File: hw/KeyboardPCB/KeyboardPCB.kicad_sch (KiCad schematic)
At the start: 176 parts, among them IC1 TPS2113ADRBR, IC2 BGM220PC22HNA2R, J1 USB_B_Micro, J2 Conn_01x07_Pin, J3 Conn_01x06_Pin, J4 Conn_02x05_Odd_Even, J5 BATT_POS, J6 BATT_NEG, K1 KEYSW, K10 KEYSW, K11 KEYSW, K12 KEYSW, K13 KEYSW, K14 KEYSW, K15 KEYSW, K16 KEYSW, K17 KEYSW, K18 KEYSW, K19 KEYSW, K2 KEYSW, K20 KEYSW, K21 KEYSW, K22 KEYSW, K23 KEYSW, K24 KEYSW, K25 KEYSW, K26 KEYSW, K27 KEYSW, K28 KEYSW, K29 KEYSW, K3 KEYSW, K30 KEYSW, K31 KEYSW, K32 KEYSW, K33 KEYSW, K34 KEYSW, K35 KEYSW, K36 KEYSW, K37 KEYSW, K38 KEYSW, K39 KEYSW, K4 KEYSW, K40 KEYSW, K41 KEYSW, K42 KEYSW, K43 KEYSW, K44 KEYSW, K45 KEYSW, K46 KEYSW, K47 KEYSW, K48 KEYSW, K49 KEYSW, K5 KEYSW, K50 KEYSW, K51 KEYSW, K52 KEYSW, K53 KEYSW, K54 KEYSW, K55 KEYSW, K56 KEYSW, K57 KEYSW, K58 KEYSW, K59 KEYSW, K6 KEYSW, K60 KEYSW, K61 KEYSW, K62 KEYSW, K7 KEYSW, K8 KEYSW, K9 KEYSW, SW2 BAT_SWITCH, U1 TM4C123GH6PMI7, U2 TPS73633DBV, U3 Adafruit ST7735R, X2 16MHz

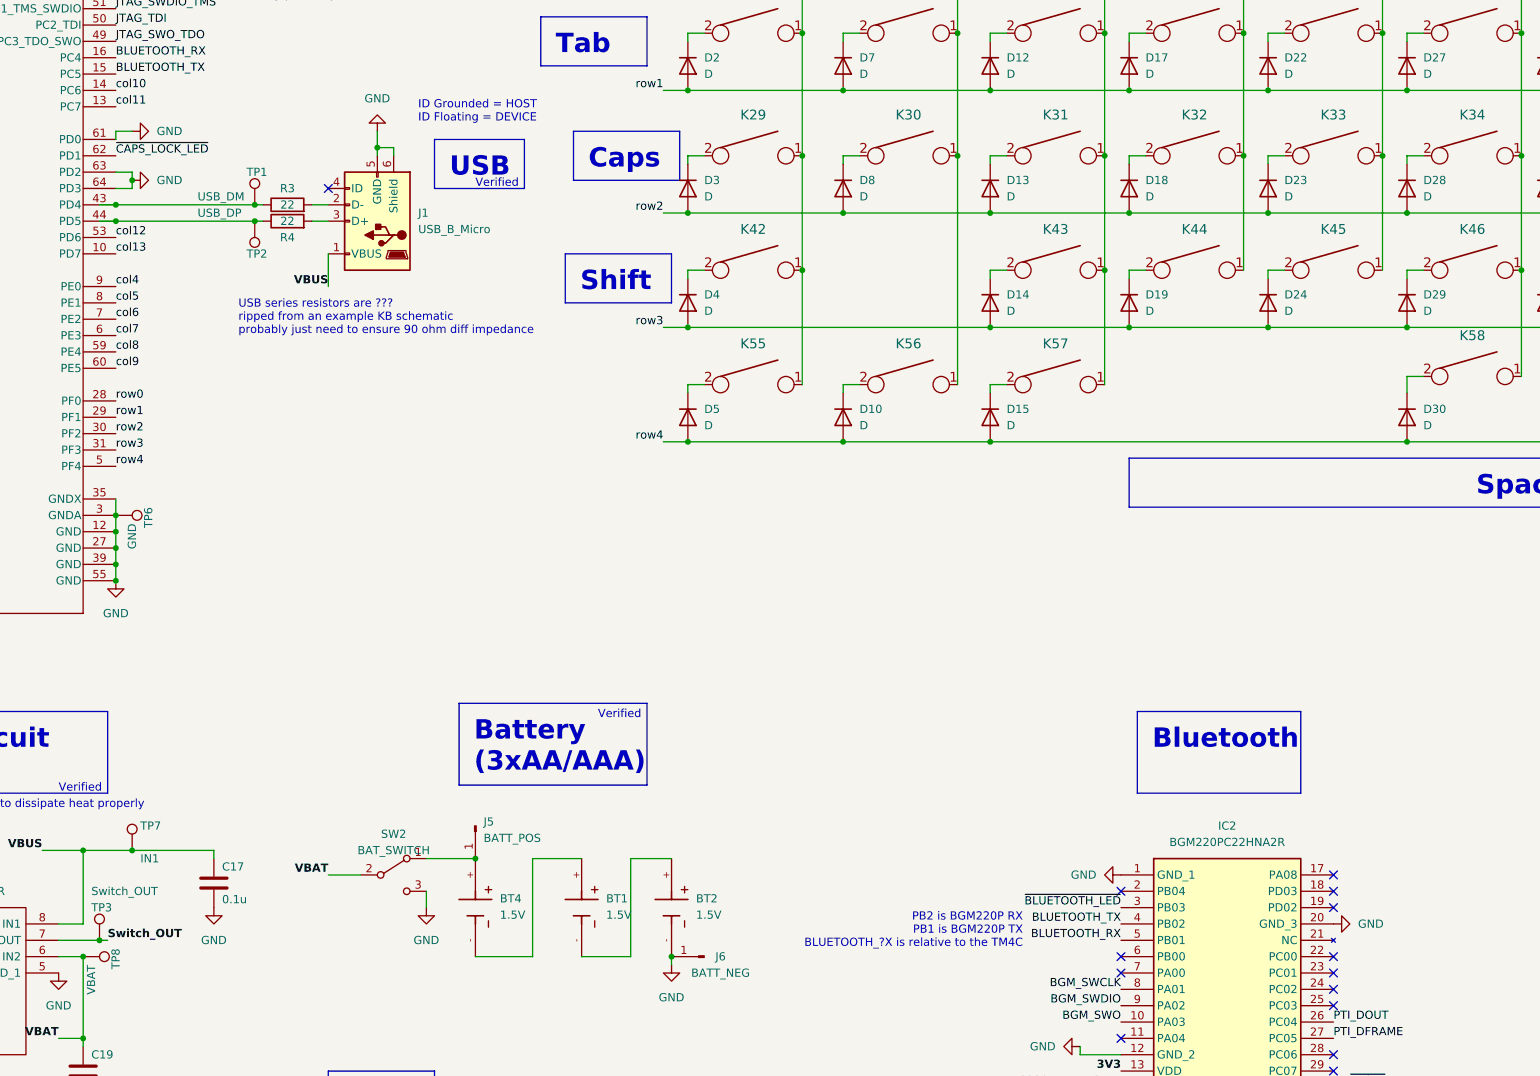
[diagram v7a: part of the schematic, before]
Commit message: Added EM4_WAKEUP signal from PD0 (TM4C) to PC0 (BGM)
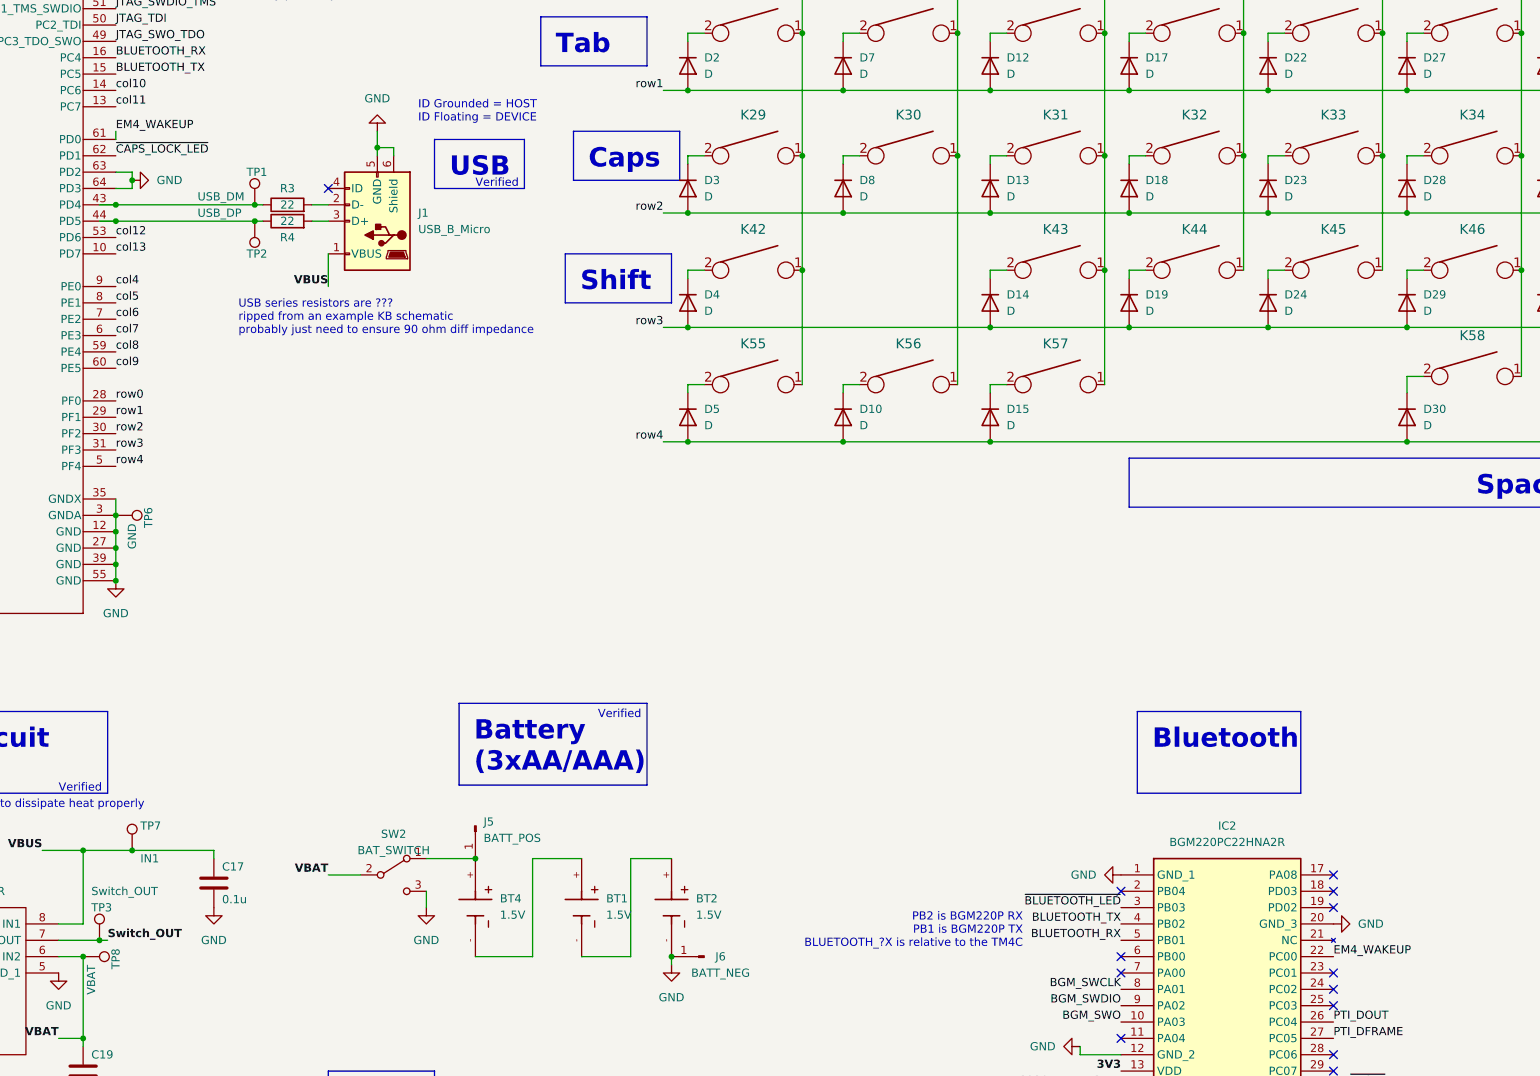
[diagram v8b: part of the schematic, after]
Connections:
- net GND: no longer U1.61 (PD0)
- net EM4_WAKEUP: now reaches IC2.22 (PC00)
- net EM4_WAKEUP: now also U1.61 (PD0)
- no-connect marks 20 -> 19
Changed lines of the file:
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@@
   (no_connect (at 200.66 127))
   (no_connect (at 323.85 236.22))
-  (no_connect (at 356.87 246.38))
   (no_connect (at 147.32 306.07))
   (no_connect (at 128.27 241.3))
@@
     (stroke (width 0) (type default))
   )
-  (wire (pts (xy 170.18 118.11) (xy 167.64 118.11))
-    (stroke (width 0) (type default))
-  )
   (wire (pts (xy 321.31 139.7) (xy 321.31 157.48))
     (stroke (width 0) (type default))
@@
     (effects (font (size 1.27 1.27)) (justify right bottom))
   )
+  (label "EM4_WAKEUP" (at 356.87 246.38 0) (fields_autoplaced)
+    (effects (font (size 1.27 1.27)) (justify left bottom))
+  )
   (label "JTAG_TDI" (at 27.94 307.34 0) (fields_autoplaced)
     (effects (font (size 1.27 1.27)) (justify left bottom))
@@
     (effects (font (size 1.27 1.27)) (justify right bottom))
   )
+  (label "EM4_WAKEUP" (at 167.64 118.11 0) (fields_autoplaced)
+    (effects (font (size 1.27 1.27)) (justify left bottom))
+  )
   (label "TM4C_DEBUG_RX" (at 96.52 312.42 0) (fields_autoplaced)
     (effects (font (size 1.27 1.27)) (justify left bottom))
@@
         )
       )
-    )
-  )
-  (symbol (lib_id "power:GND") (at 170.18 118.11 90) (unit 1)
-    (in_bom yes) (on_board yes) (dnp no) (fields_autoplaced)
-    (property "Reference" "#PWR017" (at 176.53 118.11 0)
-      (effects (font (size 1.27 1.27)) hide)
-    )
-    (property "Value" "GND" (at 173.99 118.11 90)
-      (effects (font (size 1.27 1.27)) (justify right))
-    )
-    (property "Footprint" "" (at 170.18 118.11 0)
-      (effects (font (size 1.27 1.27)) hide)
-    )
-    (property "Datasheet" "" (at 170.18 118.11 0)
-      (effects (font (size 1.27 1.27)) hide)
-    )
-    (pin "1")
-    (instances
-      (project "KeyboardPCB"
-        (path "/2d193c8d-36cd-4337-adc1-05f8d95a4b88"
-          (reference "#PWR017") (unit 1)
-        )
-      )
